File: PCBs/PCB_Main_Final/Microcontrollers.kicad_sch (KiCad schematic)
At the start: 20 parts, among them U7 ESP32-WROOM-E, U8 ESP32-WROVER-E

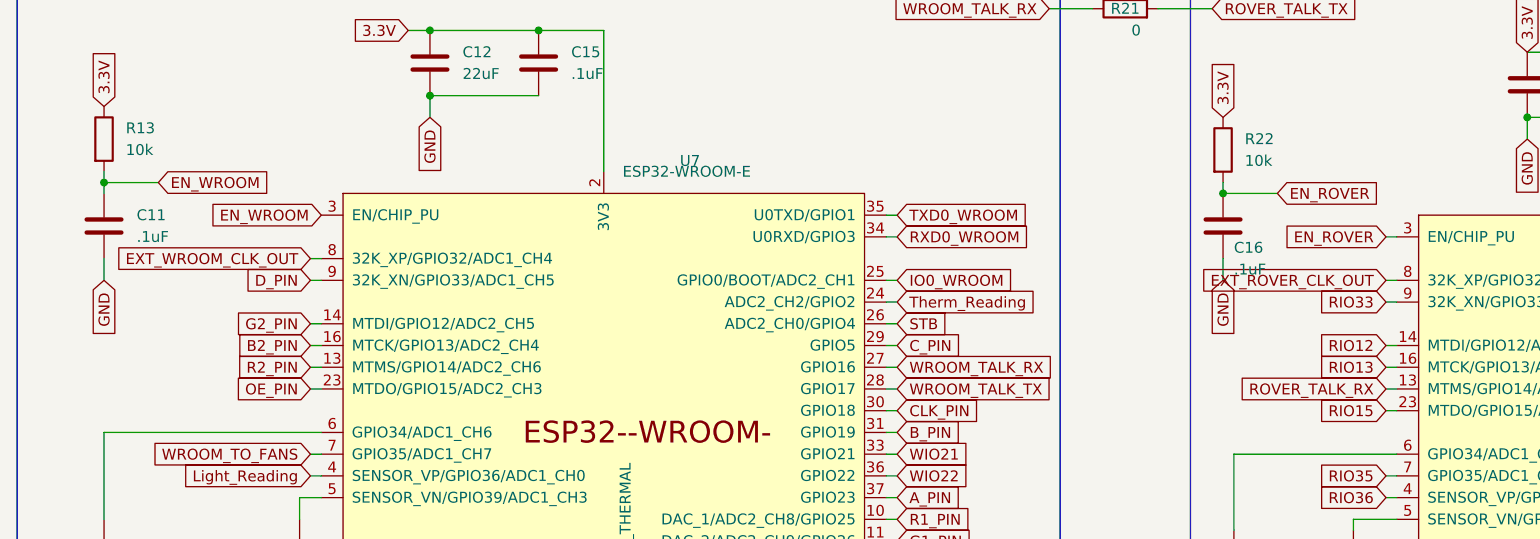
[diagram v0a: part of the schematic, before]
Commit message: finished Main and Light Sensor PCBs
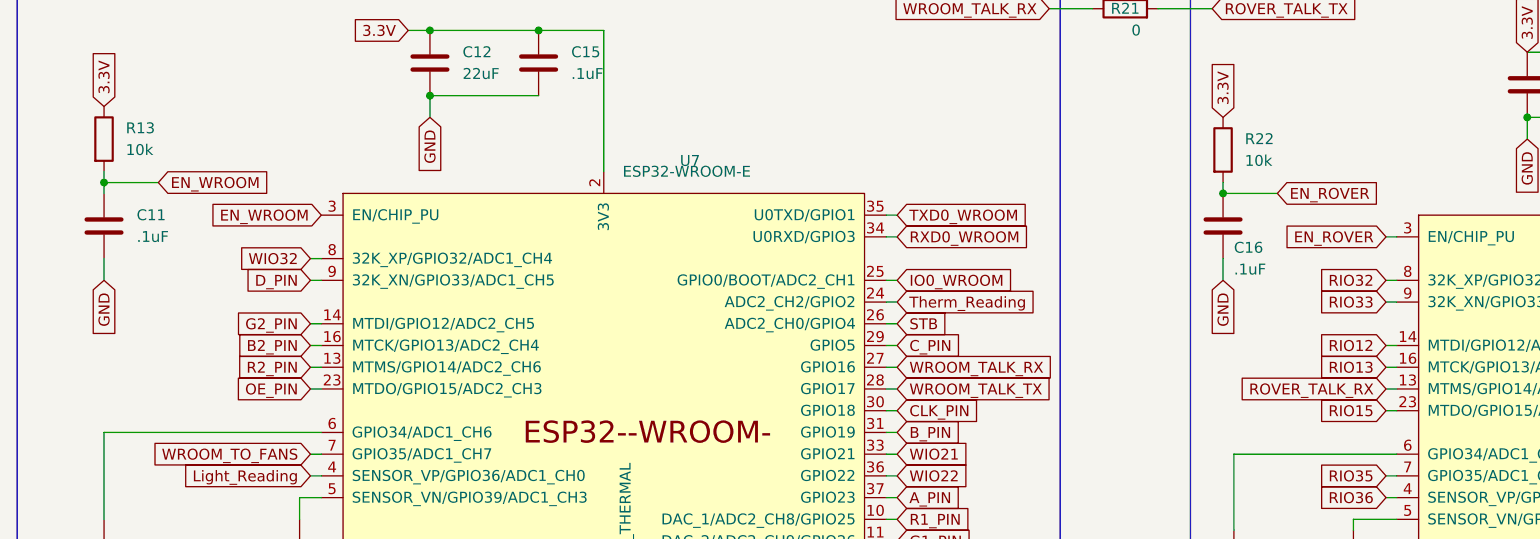
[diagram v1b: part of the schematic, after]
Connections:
- net EXT_ROVER_CLK_OUT renamed RIO32
- net EXT_WROOM_CLK_OUT renamed WIO32
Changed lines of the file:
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@@
     )
   )
-  (global_label "EXT_ROVER_CLK_OUT" (shape input) (at 175.26 95.25 180) (fields_autoplaced)
-    (effects (font (size 1.27 1.27)) (justify right))
-    (property "Intersheetrefs" "${INTERSHEET_REFS}" (at 152.7411 95.25 0)
+  (global_label "RIO32" (shape input) (at 175.26 95.25 180) (fields_autoplaced)
+    (effects (font (size 1.27 1.27)) (justify right))
+    (property "Intersheetrefs" "${INTERSHEET_REFS}" (at 166.6505 95.25 0)
       (effects (font (size 1.27 1.27)) (justify right) hide)
     )
@@
     )
   )
-  (global_label "EXT_WROOM_CLK_OUT" (shape input) (at 49.53 92.71 180) (fields_autoplaced)
-    (effects (font (size 1.27 1.27)) (justify right))
-    (property "Intersheetrefs" "${INTERSHEET_REFS}" (at 26.2854 92.71 0)
-      (effects (font (size 1.27 1.27)) (justify right) hide)
-    )
+  (global_label "WIO32" (shape input) (at 49.53 92.71 180) (fields_autoplaced)
+    (effects (font (size 1.27 1.27)) (justify right))
+    (property "Intersheetrefs" "${INTERSHEET_REFS}" (at 40.7391 92.71 0)
+      (effects (font (size 1.27 1.27)) (justify right) hide)
+    )
